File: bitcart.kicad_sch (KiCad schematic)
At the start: 4 parts

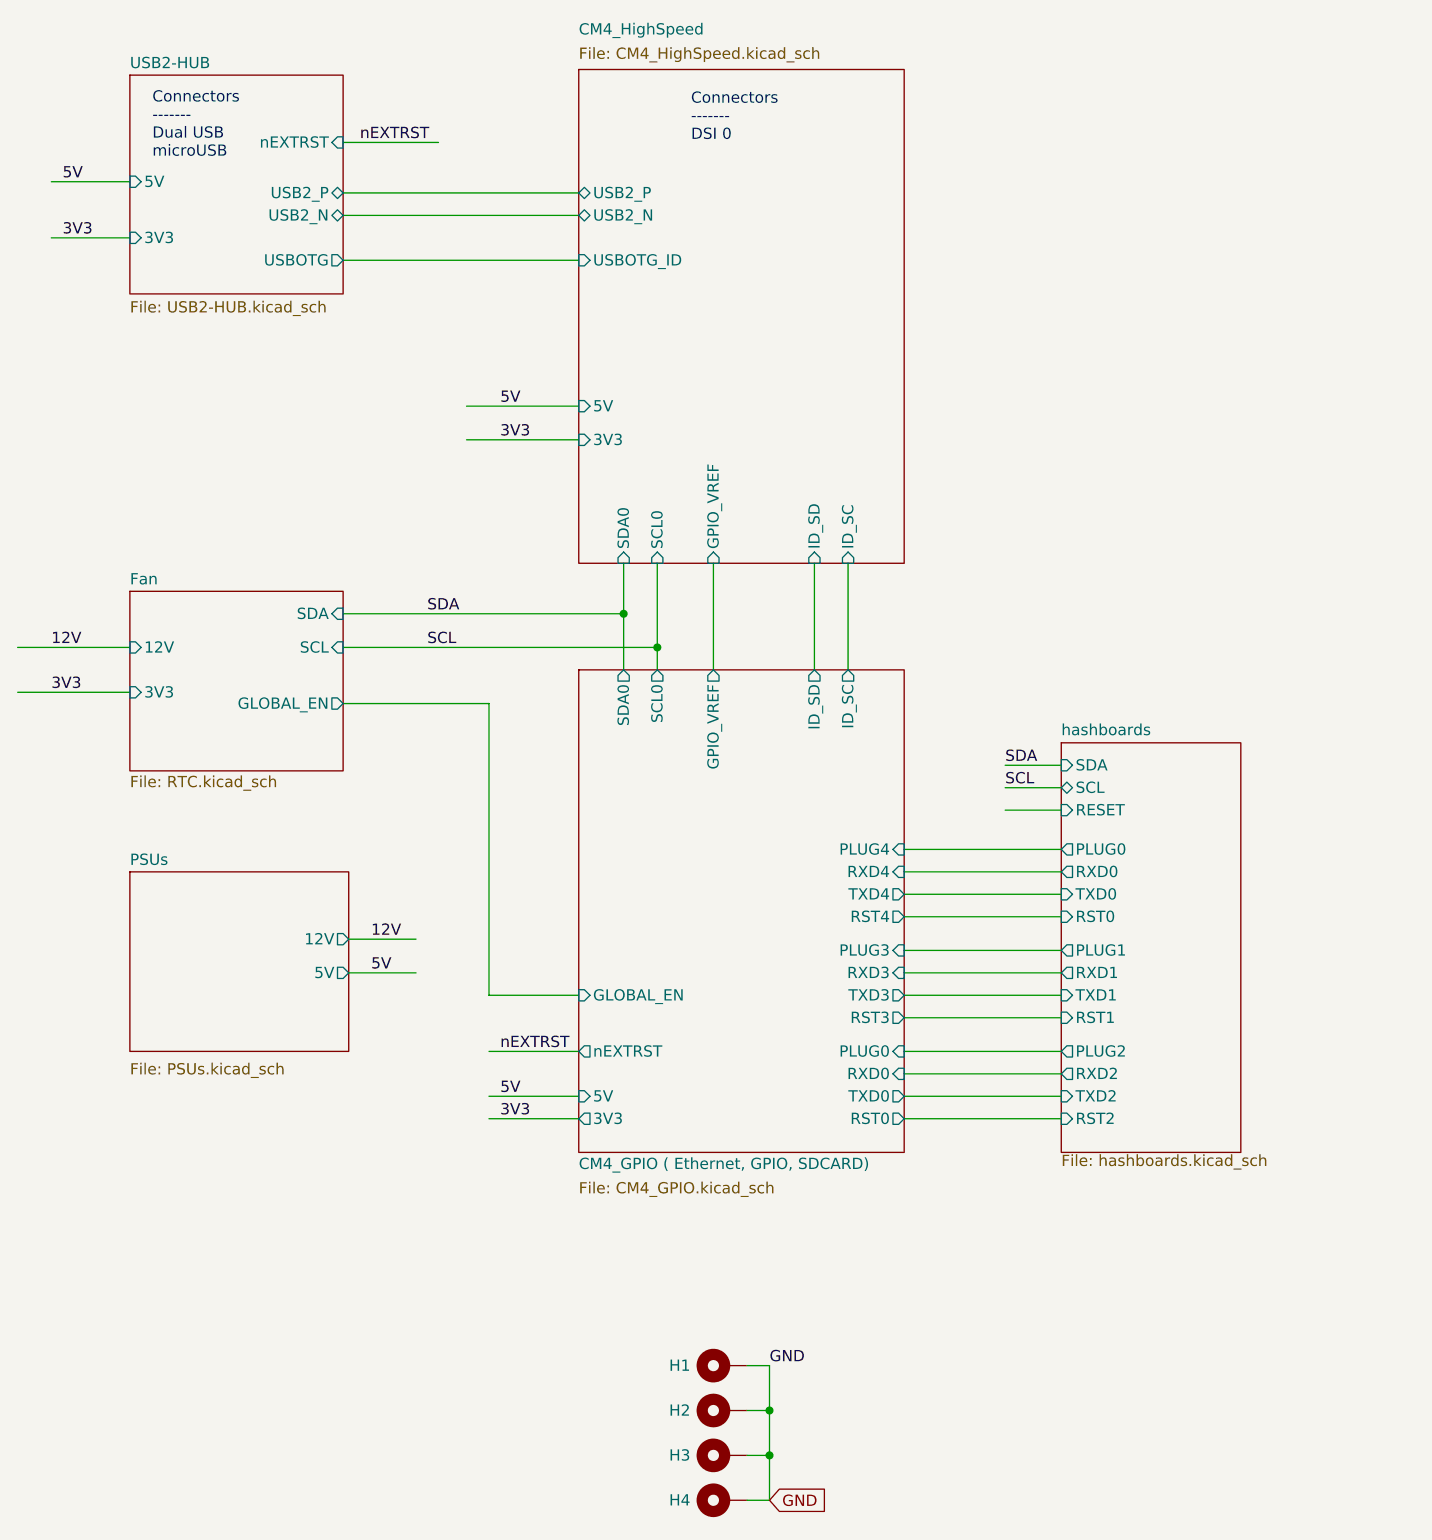
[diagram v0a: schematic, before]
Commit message: added more USB ports.. placing
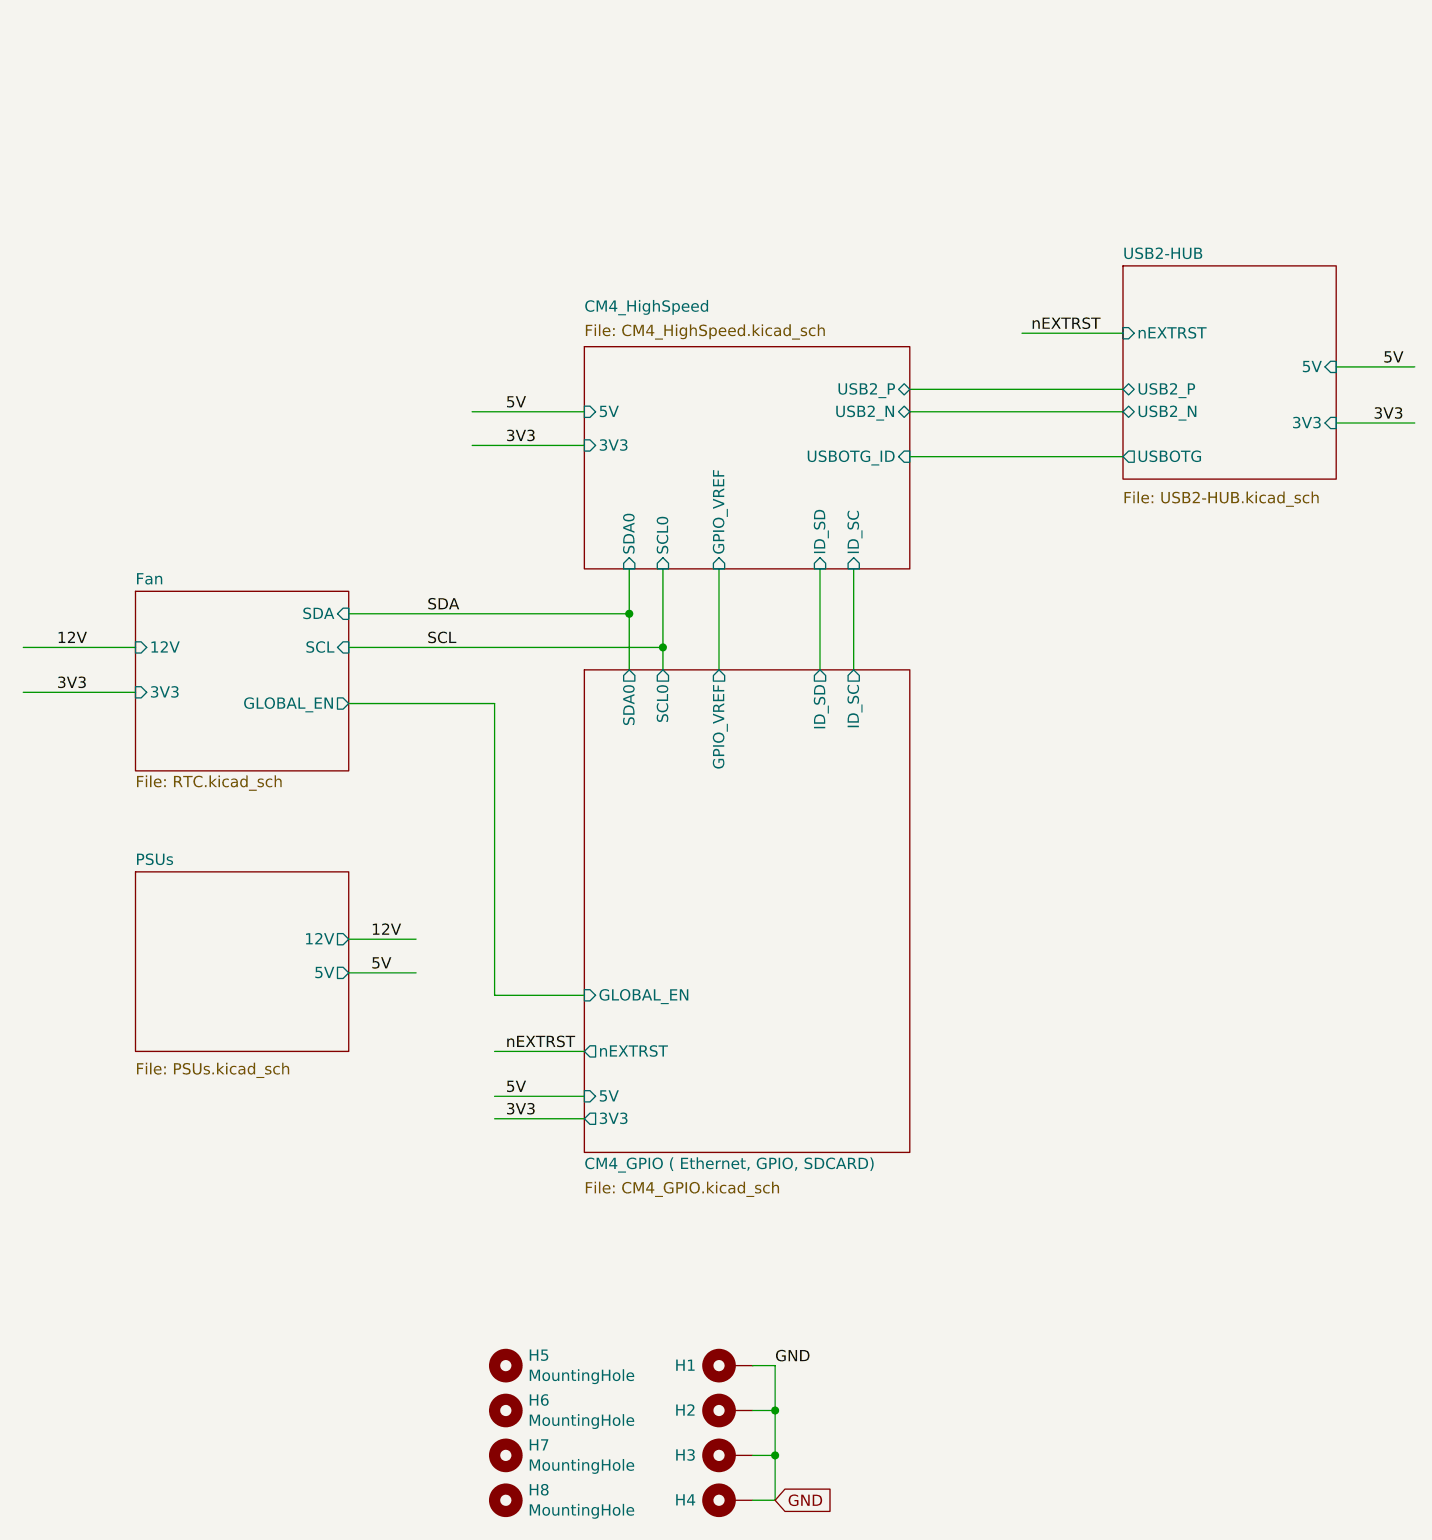
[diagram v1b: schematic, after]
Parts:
- added H5, H6, H7, H8: MountingHole, MountingHole:MountingHole_2.7mm_M2.5, symbol Mechanical:MountingHole
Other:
- removed sheet hashboards
- sheet CM4_GPIO ( Ethernet, GPIO, SDCARD) ports: added none; removed PLUG0, PLUG3, PLUG4, RST0, RST3, RST4, RXD0, RXD3, RXD4, TXD0, TXD3, TXD4
- note removed: "Connectors ------- DSI 0"
- note removed: "Connectors ------- Dual USB microUSB"
- moved on the sheet: H1, H2, H3, H4
